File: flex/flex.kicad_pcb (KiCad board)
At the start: 2 copper layers, 126.3 x 91.6 mm, 91 parts, among them J1 Conn_01x04_Female, J2 Conn_01x05_Female, J3 Conn_01x03_Female, J4 Conn_01x06_Female, J5 Conn_01x03_Female, SW10 SW_Push, SW11 SW_Push, SW12 SW_Push, SW15 SW_Push, SW16 SW_Push, SW17 SW_Push, SW2 SW_Push, SW20 SW_Push, SW21 SW_Push, SW22 SW_Push, SW24 SW_Push, SW25 SW_Push, SW26 SW_Push, SW3 SW_Push, SW4 SW_Push, SW6 SW_Push, SW7 SW_Push, SW8 SW_Push

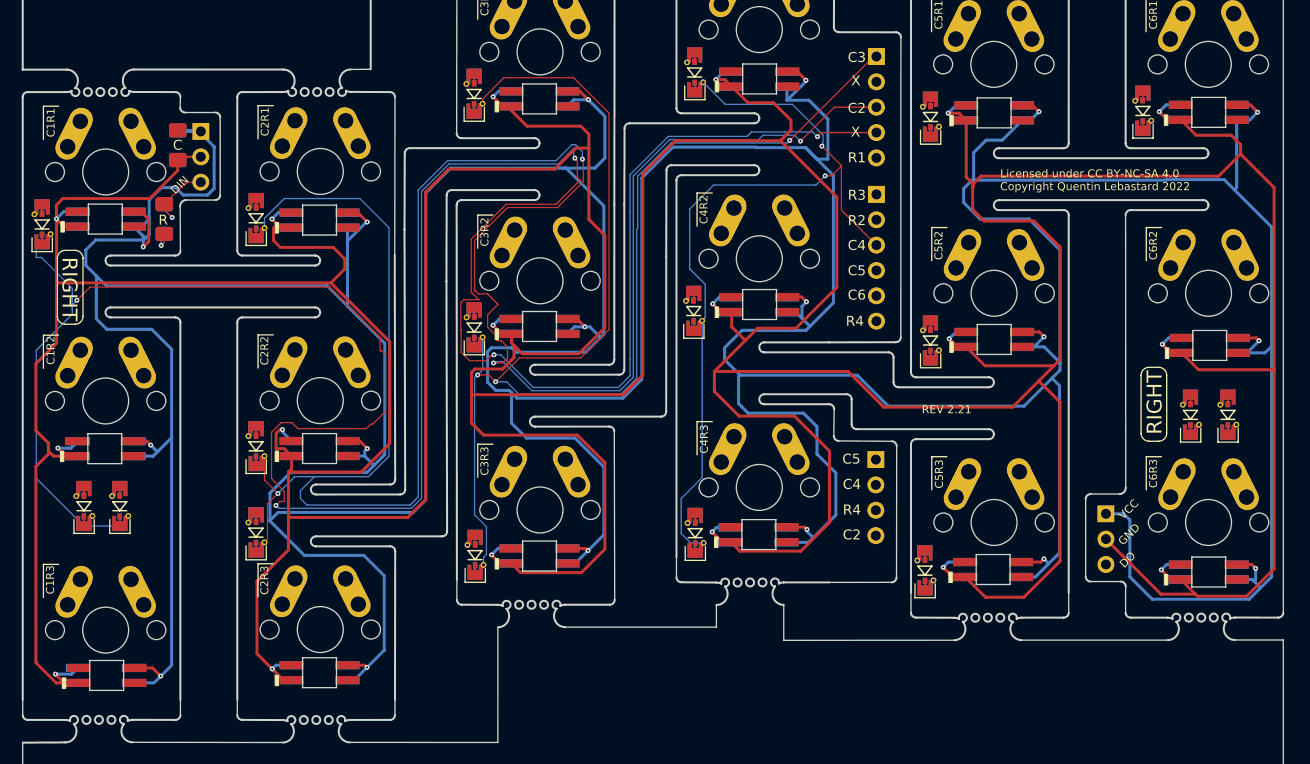
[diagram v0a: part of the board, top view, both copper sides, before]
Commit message: rgb leds gnd silkscreen
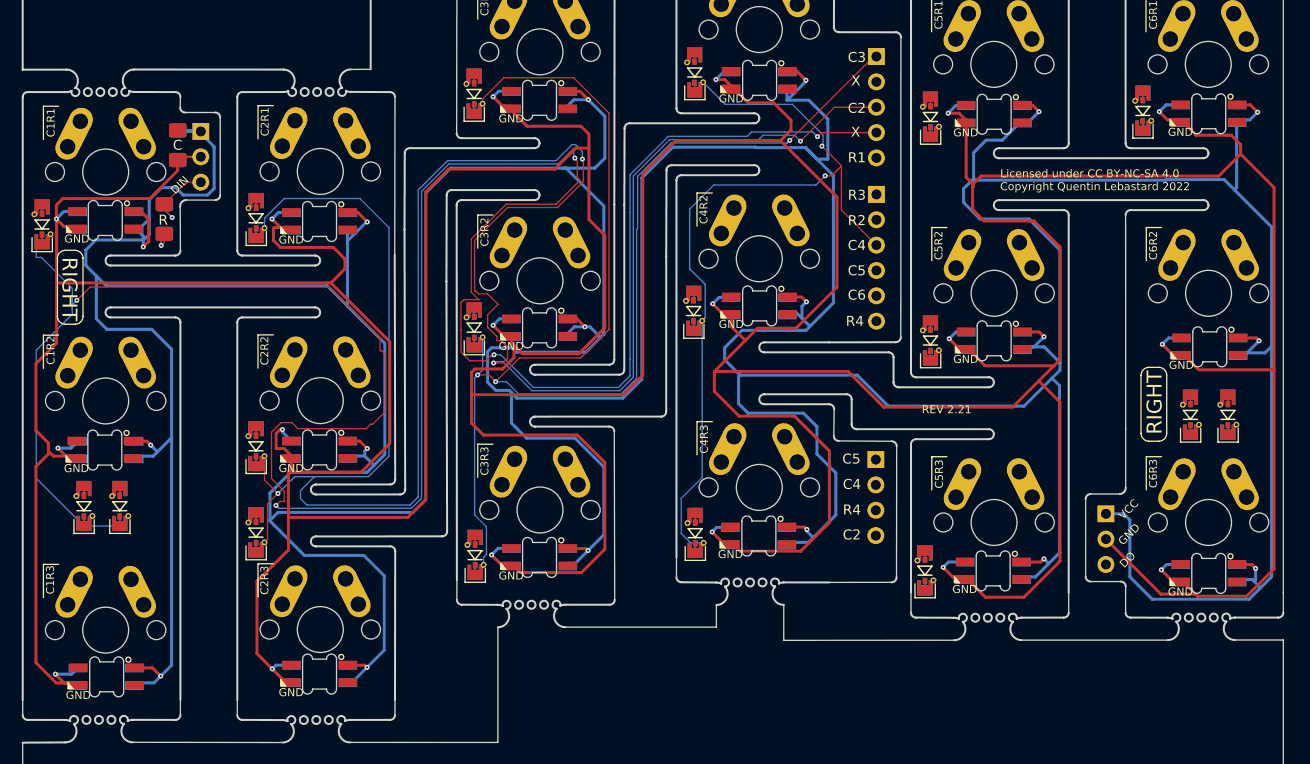
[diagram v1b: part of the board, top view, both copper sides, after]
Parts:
- D18, D21, D23, D25, D3, D33, D37, D39, D4, D41, D47, D49, D5, D51, D55, D57, D59, D7: footprint libs2:YS-SK6812MINI-E_REVERSE -> custom:SK6812_mini_e_corners
- D22, D24, D26, D28, D29, D30, D34, D38, D40, D42, D48, D50, D52, D56, D58, D6, D60, D8: footprint libs2:YS-SK6812MINI-E_REVERSE_NO_EDGECUT -> custom:SK6812_mini_e_corners_NOEDGECUTS
- moved D34 0.25 mm to (65.2, 83.4)
- moved D38 0.25 mm to (109.2, 114.9)
- moved D48 0.25 mm to (132.8, 72.6)
- moved D50 0.25 mm to (132.8, 95.3)
- moved D52 0.25 mm to (132.7, 118.4)
- moved D56 0.25 mm to (154.3, 72.6)
- moved D58 0.25 mm to (154.4, 95.9)
- moved D6 0.25 mm to (65.2, 128.7)
- moved D60 0.25 mm to (154.3, 118.6)
- moved D8 0.25 mm to (65.2, 106.2)
- moved D28 0.25 mm to (43.8, 83.3)
- moved D29 0.25 mm to (43.8, 106.3)
- moved D30 0.25 mm to (43.8, 129.0)
- moved D22 0.25 mm to (87.2, 71.2)
- moved D24 0.25 mm to (87.2, 94.0)
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
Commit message: routing
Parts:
- moved D28 0.08 mm to (43.9, 83.3)
- moved D29 0.08 mm to (43.9, 106.3)
- moved D30 0.08 mm to (43.9, 129.0)
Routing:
- net col6: track 5.75 -> 197.9 mm, vias 0 -> 3
- net col5: track 5.75 -> 85.3 mm, vias 0 -> 1
- net Vcc: track 725.8 -> 735.0 mm
- net Gnd: track 754.7 -> 757.6 mm

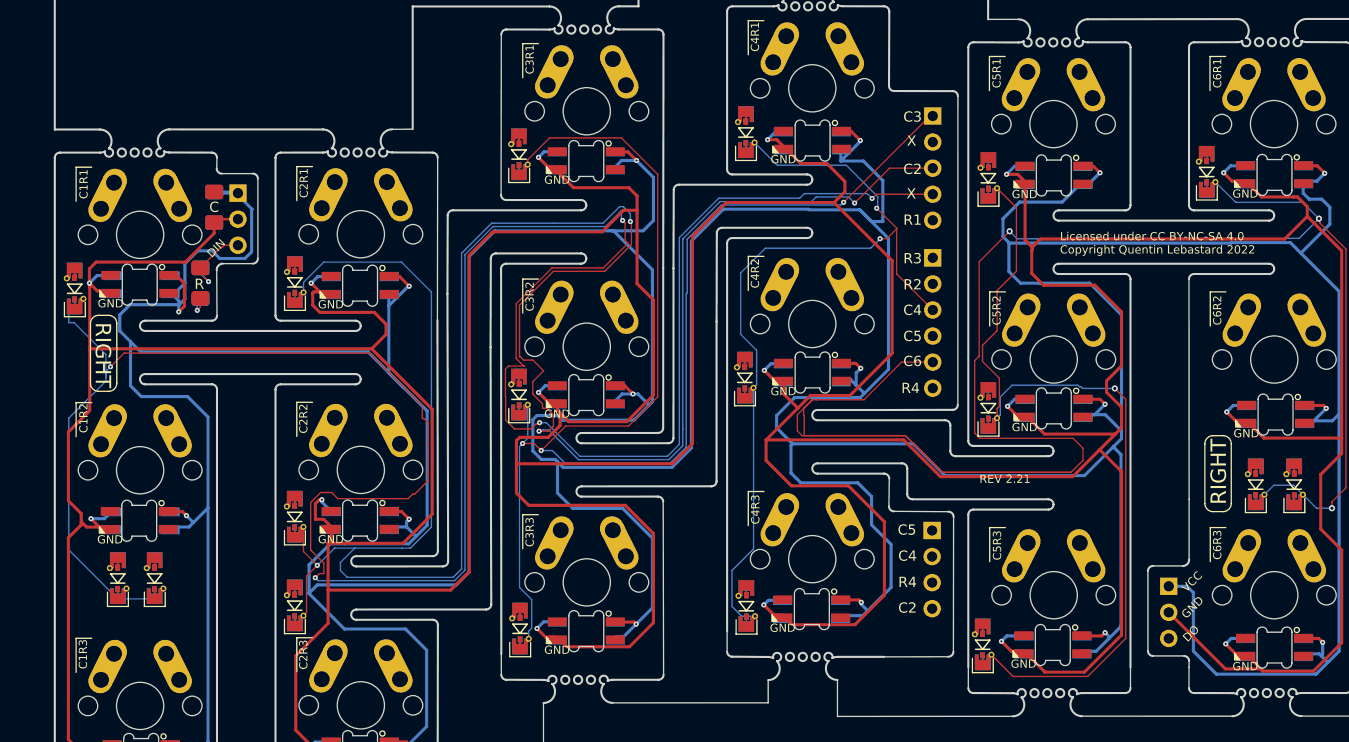
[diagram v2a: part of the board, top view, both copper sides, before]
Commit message: diode routing
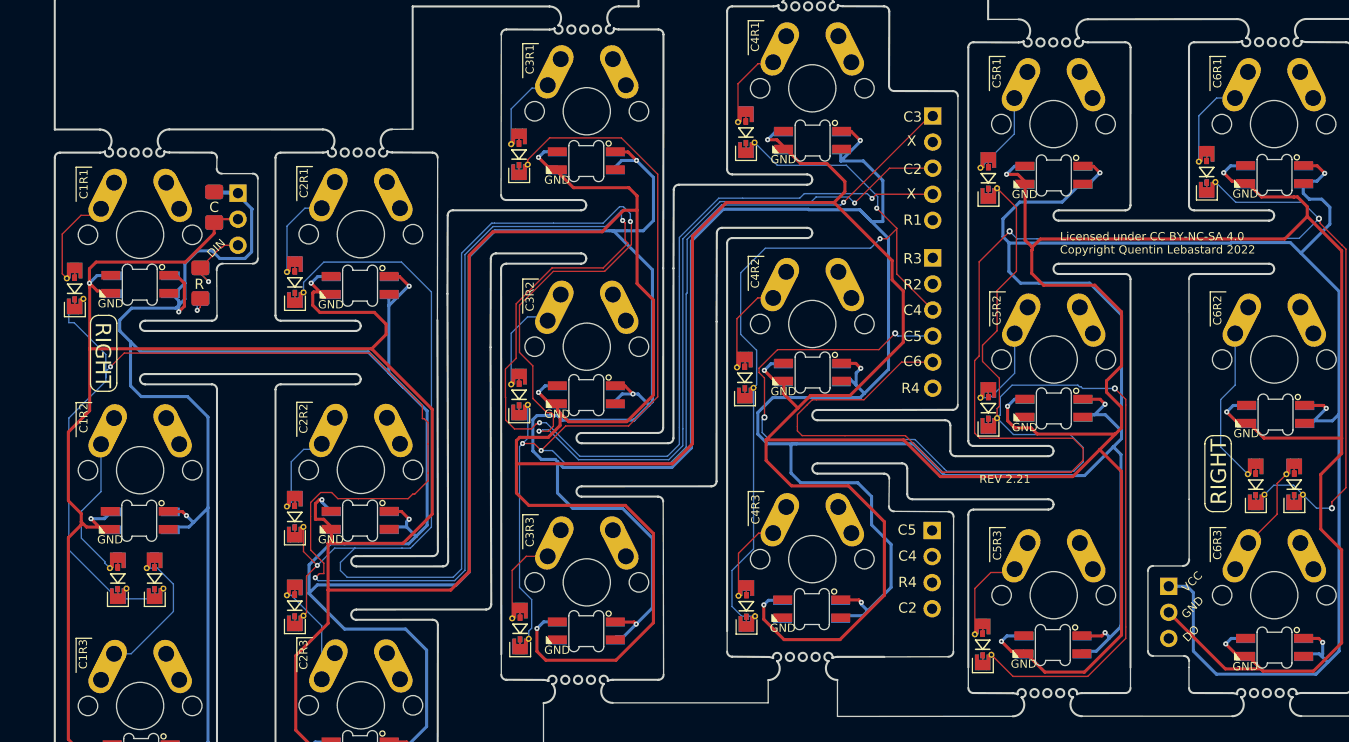
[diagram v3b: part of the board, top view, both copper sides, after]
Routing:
- net col5: track 85.3 -> 154.6 mm, vias 1 -> 3
- net col6: track 197.9 -> 179.2 mm
- net Net-(D36-A): track 1.92 -> 17.3 mm
- net Net-(D10-A): track 1.92 -> 15.9 mm
- net Net-(D1-A): track 1.92 -> 15.3 mm
- net Net-(D12-A): track 1.92 -> 11.8 mm
- net Net-(D19-A): track 1.92 -> 11.3 mm
- net Net-(D2-A): track 1.92 -> 11.2 mm
- net Net-(D31-A): track 1.92 -> 11.0 mm
- net Net-(D27-A): track 1.92 -> 11.0 mm
- net Net-(D17-A): track 1.92 -> 10.6 mm
- net Net-(D16-A): track 1.92 -> 10.6 mm
- net Net-(D9-A): track 1.92 -> 10.5 mm
- net Net-(D20-A): track 1.92 -> 10.2 mm
- net Net-(D35-A): track 1.92 -> 10.2 mm
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
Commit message: routing
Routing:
- net row4: track 0.00 -> 468.8 mm, vias 0 -> 10
- net row3: track 0.00 -> 360.5 mm, vias 0 -> 11
- net row2: track 0.00 -> 225.6 mm, vias 0 -> 3
- net Vcc: track 739.3 -> 759.5 mm
- net Gnd: track 763.7 -> 776.8 mm
- net col4: track 87.0 -> 91.8 mm
- net col5: track 154.6 -> 157.2 mm
- net col2: track 226.2 -> 228.3 mm
- net col6: track 179.2 -> 177.2 mm
- net col3: track 146.7 -> 147.8 mm
- net col1: track 264.2 -> 265.0 mm

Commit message: routing
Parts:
- removed the SW10 at (-69.9, 58.5)
- removed the SW11 at (-69.9, 81.4)
- removed the SW12 at (-69.9, 104.4)
- removed the SW15 at (-48.0, 56.3)
- removed the SW16 at (-48.0, 79.2)
- removed the SW17 at (-48.0, 102.1)
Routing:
- net Net-(D18-DOUT): track 0.00 -> 126.3 mm, vias 0 -> 4
- net Net-(D28-DOUT): track 0.00 -> 42.2 mm, vias 0 -> 4
- net Net-(D18-DIN): track 0.00 -> 39.9 mm, vias 0 -> 2
- net Net-(D28-DIN): track 2.57 -> 17.7 mm, vias 1 -> 3
- net Vcc: track 759.5 -> 754.1 mm
- net Gnd: track 776.8 -> 781.9 mm
- net Net-(D5-DOUT): track 0.00 -> 3.54 mm, vias 0 -> 1
- net row4: track 468.8 -> 469.4 mm
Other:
- board text removed: "GITHUB.COM/BASTARDKB"
